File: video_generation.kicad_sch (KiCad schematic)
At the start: 34 parts, among them J12 28L22, J15 74LS161, K15 74LS04

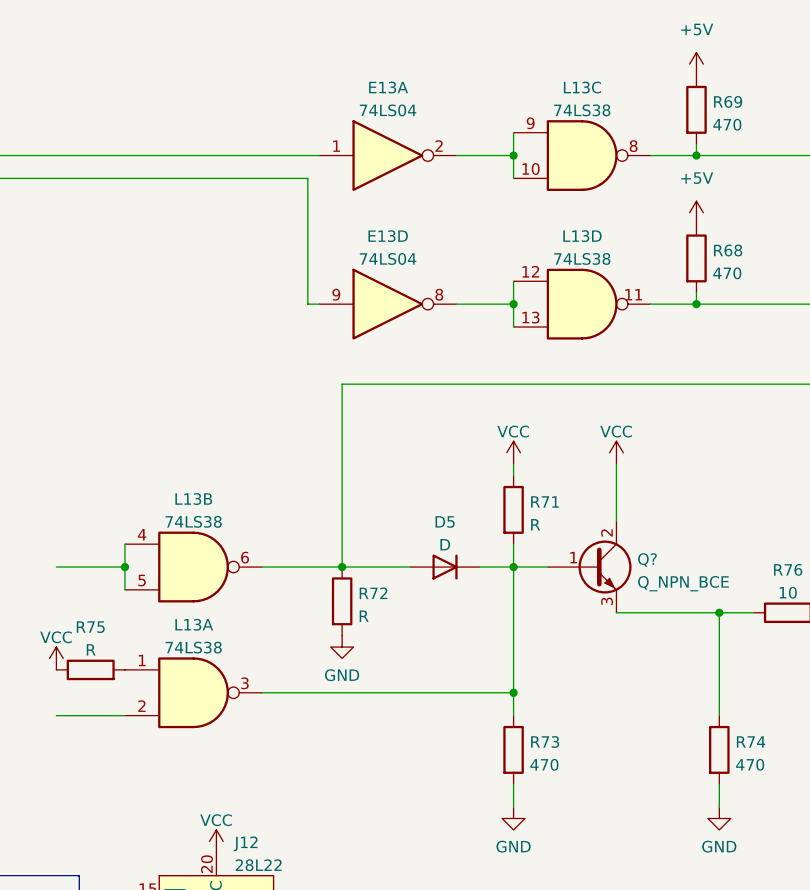
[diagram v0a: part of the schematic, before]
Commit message: Upgraded to kicad 7
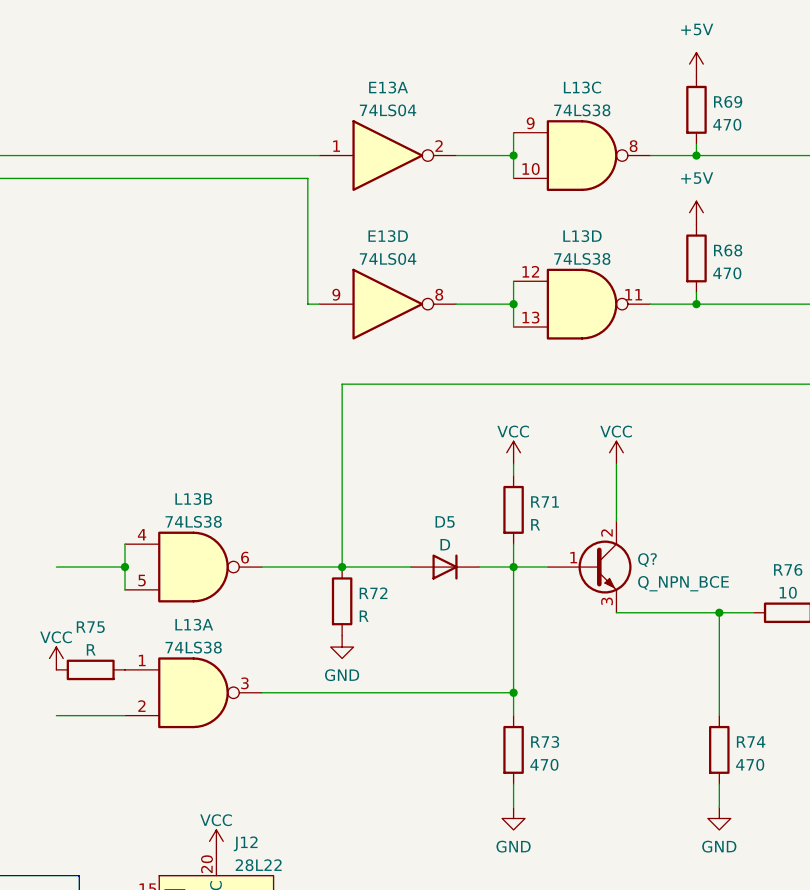
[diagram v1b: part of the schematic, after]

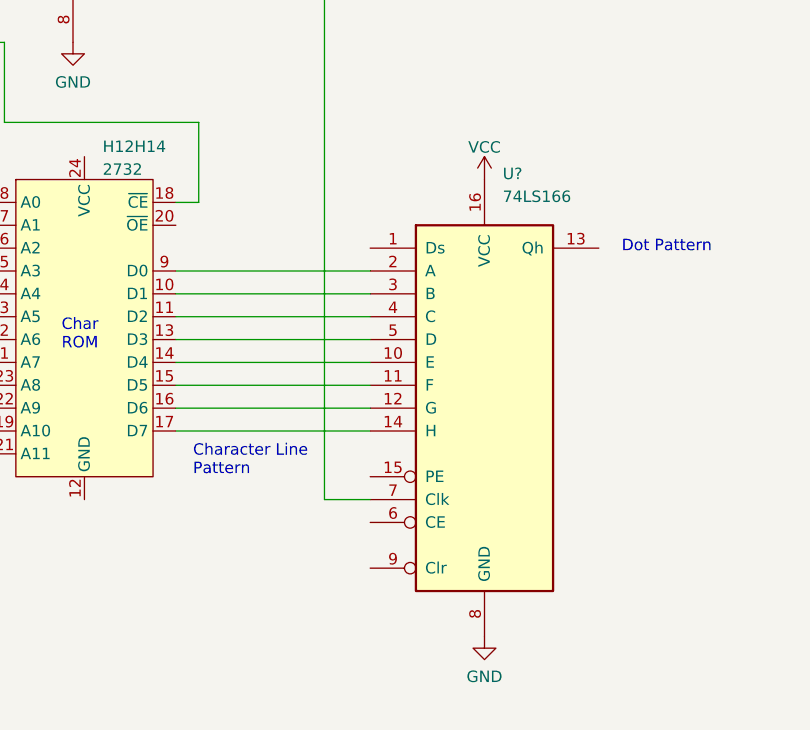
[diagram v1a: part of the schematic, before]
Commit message: Note in pixel shift register
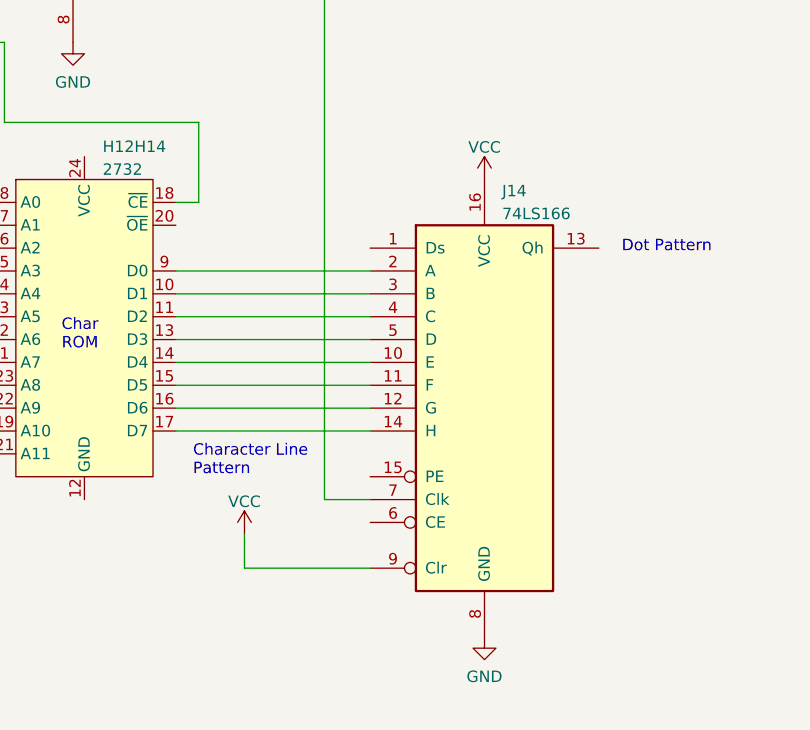
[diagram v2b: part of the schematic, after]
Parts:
- gave numbers to parts that had none: 1
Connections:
- net VCC: now also J14.9 (Clr)
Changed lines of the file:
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@@
+    (stroke (width 0) (type default))
+  )
+  (wire (pts (xy 252.73 198.12) (xy 238.76 198.12))
     (stroke (width 0) (type default))
   )
@@
   )
   (bus (pts (xy 25.4 238.76) (xy 25.4 246.38))
+    (stroke (width 0) (type default))
+  )
+  (wire (pts (xy 238.76 194.31) (xy 238.76 198.12))
     (stroke (width 0) (type default))
   )
@@
         (path "/12a6dbe3-008d-4c5b-88f6-9f1c816060be/ce60e45b-d802-4380-8f39-bef3de5fa20e"
           (reference "K15") (unit 4)
+        )
+      )
+    )
+  )
+  (symbol (lib_id "power:VCC") (at 238.76 194.31 0) (unit 1)
+    (in_bom yes) (on_board yes) (dnp no)
+    (property "Reference" "#PWR01" (at 238.76 198.12 0)
+      (effects (font (size 1.27 1.27)) hide)
+    )
+    (property "Value" "VCC" (at 238.76 190.7342 0)
+      (effects (font (size 1.27 1.27)))
+    )
+    (property "Footprint" "" (at 238.76 194.31 0)
+      (effects (font (size 1.27 1.27)) hide)
+    )
+    (property "Datasheet" "" (at 238.76 194.31 0)
+      (effects (font (size 1.27 1.27)) hide)
+    )
+    (pin "1")
+    (instances
+      (project "ceda"
+        (path "/12a6dbe3-008d-4c5b-88f6-9f1c816060be/ce60e45b-d802-4380-8f39-bef3de5fa20e"
+          (reference "#PWR01") (unit 1)
         )
       )
@@
   (symbol (lib_id "74xx:74LS166") (at 265.43 180.34 0) (unit 1)
     (in_bom yes) (on_board yes) (dnp no) (fields_autoplaced)
-    (property "Reference" "U?" (at 267.4494 154.305 0)
-      (effects (font (size 1.27 1.27)) (justify left))
-    )
-    (property "Value" "74LS166" (at 267.4494 156.845 0)
+    (property "Reference" "J14" (at 267.3859 156.21 0)
+      (effects (font (size 1.27 1.27)) (justify left))
+    )
+    (property "Value" "74LS166" (at 267.3859 158.75 0)
       (effects (font (size 1.27 1.27)) (justify left))
     )
@@
       (project "ceda"
         (path "/12a6dbe3-008d-4c5b-88f6-9f1c816060be/ce60e45b-d802-4380-8f39-bef3de5fa20e"
-          (reference "U?") (unit 1)
-        )
-      )
+          (reference "J14") (unit 1)
+        )
+      )

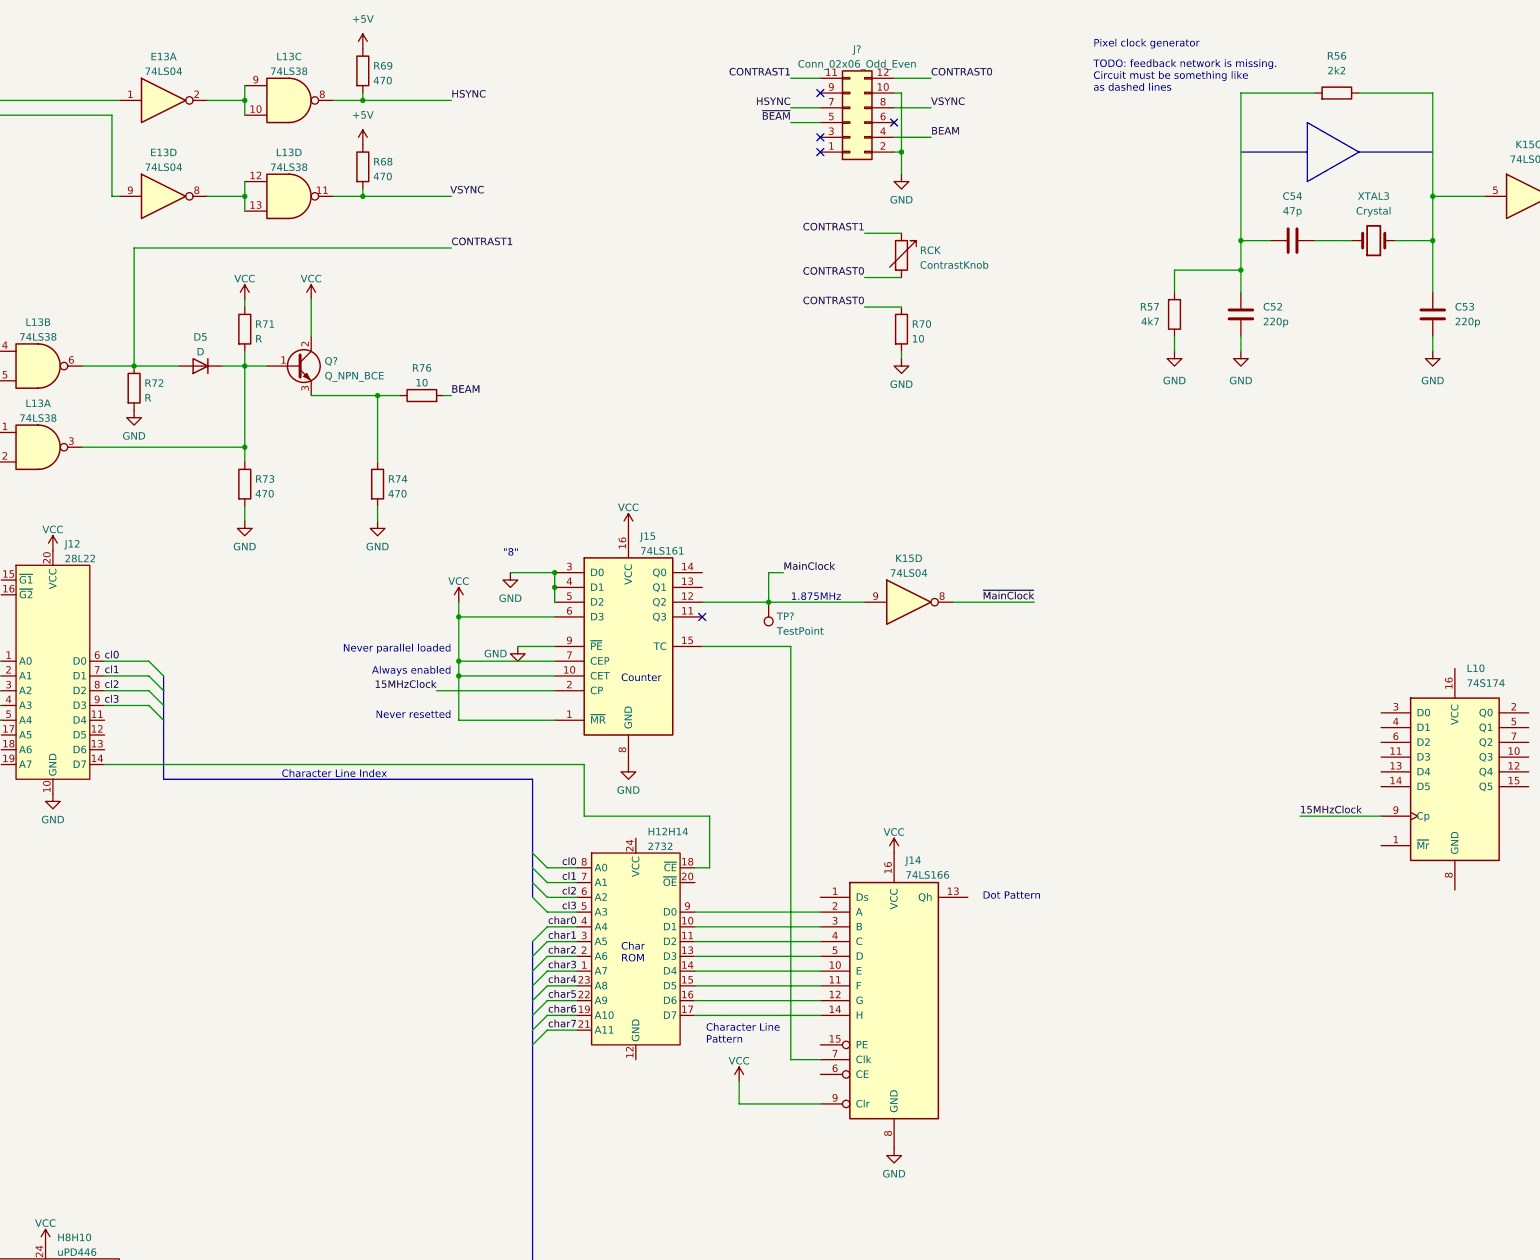
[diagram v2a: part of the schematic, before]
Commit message: Discovered bank 0 + fixed wrong signals in video gen
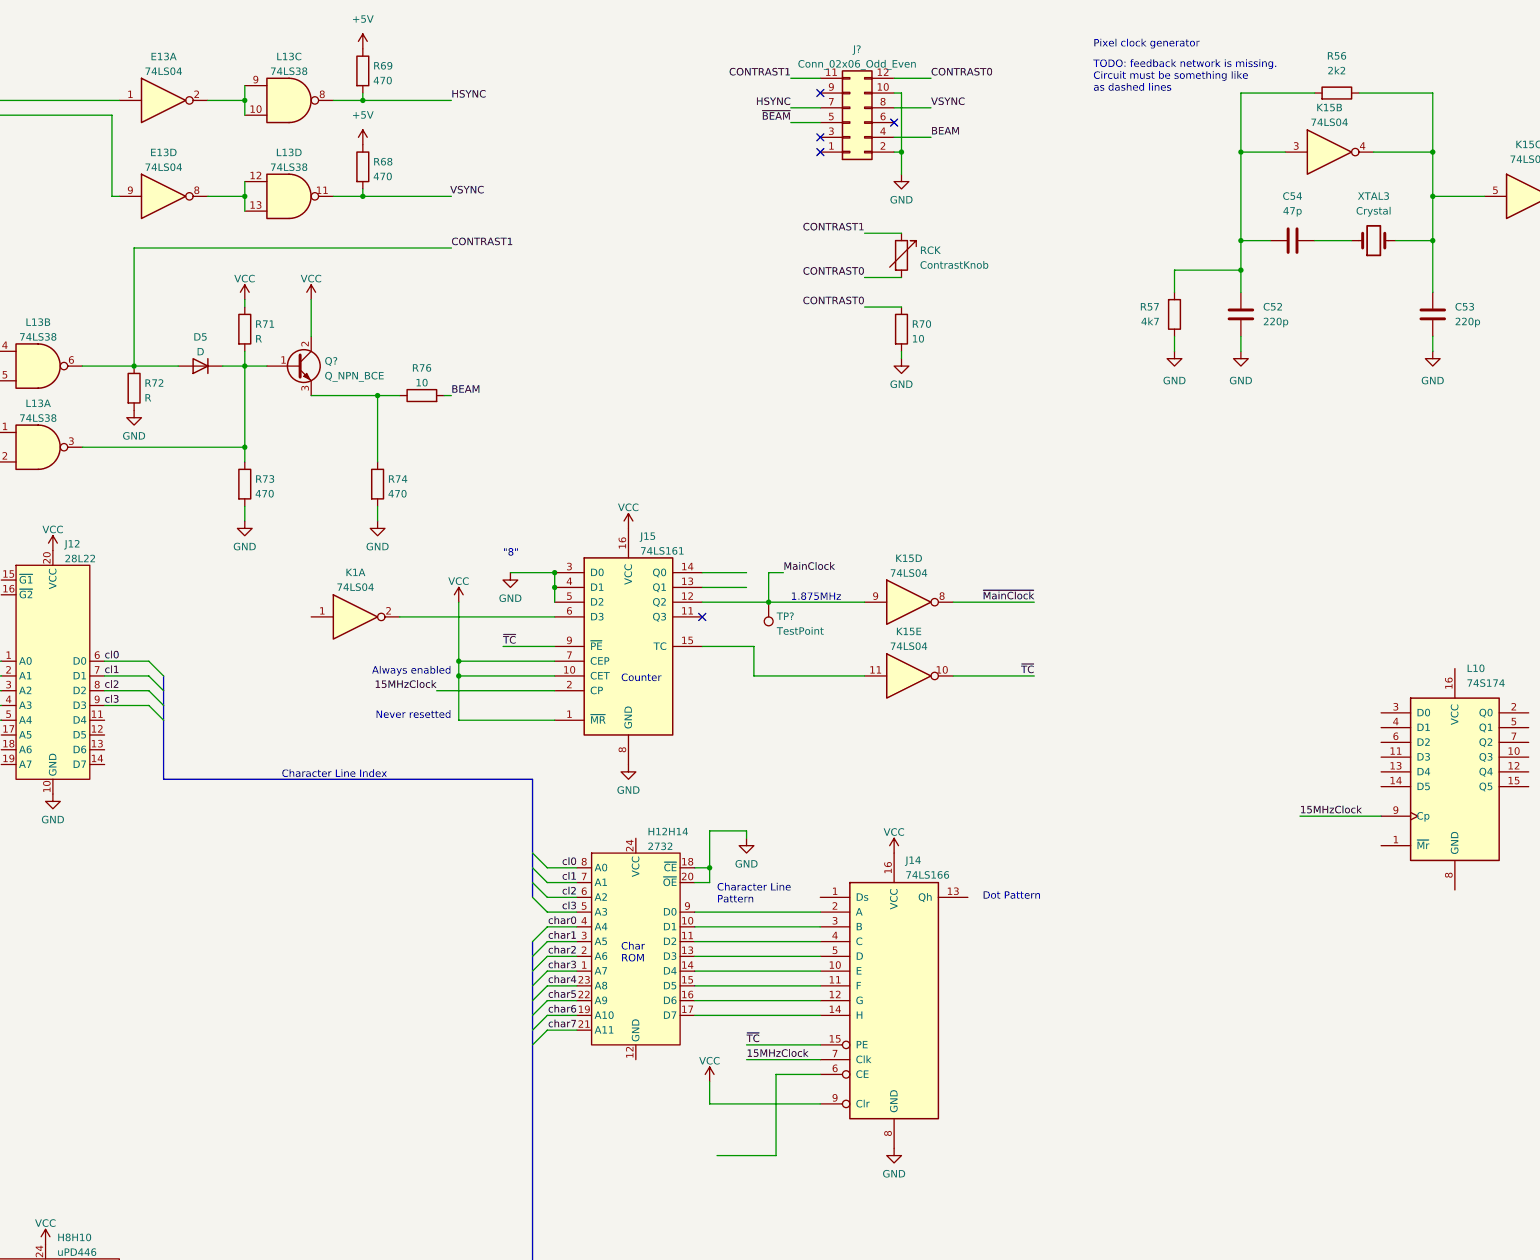
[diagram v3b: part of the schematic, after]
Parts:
- added K1: 74LS04, symbol 74xx:74LS04
- added unit 2 of K15
- added unit 5 of K15
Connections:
- net 15MHzClock: now also J14.7 (Clk)
- net GND: now also H12H14.18 (~{CE}), H12H14.20 (~{OE}); no longer J15.9 (~{PE})
- net VCC: no longer J15.6 (D3)
- net at J12.14 (D7): no longer H12H14.18 (~{CE})
- net at C53.1, K15.5, R56.1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: now also K15.4
- net at C52.1, C54.2, R56.2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: now also K15.3
- net at J15.15 (TC): now also K15.11; no longer J14.7 (Clk)
- net ~{TC}: now reaches J14.15 (PE)
- net ~{TC}: now also J15.9 (~{PE}), K15.10
- new net: J15.6 (D3), K1.2
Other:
- note removed: "Never parallel loaded"

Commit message: A long job in analog video output
! Read comments inside video_memory_management sheet for more
informations.

- Completed path between dot pattern output of character shift register
and beam output transistor.
- Found behavior of video attribute signals: blink, underline, stretch,
  hide.
- Completed wiring of 28L22 ROM, which is involved in video attributes.
- TODO: video_memory_management must be cleaned up, since schematics has grown
outside sheet.
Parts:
- added D2: D, symbol Device:D
- added E12: 74LS175, symbol 74xx:74LS175
- added J13: 74LS86, symbol 74xx:74LS86
- added K0000, L12, U14, U5: 74LS00, symbol 74xx:74LS00
- added K10, U3: 74LS08, symbol 74xx:74LS08
- added K11, K12: 74LS273, symbol 74xx:74LS273
- added K14, U2: 74LS10, symbol 74xx:74LS10
- added R67, R71: R, symbol Device:R
- added U1: 74LS393, symbol 74xx:74LS393
- added U4: 74LS04, symbol 74xx:74LS04
- gave numbers to parts that had none: 1
- renumbered K1 to K15
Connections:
- net GND: now also R71.2
- net MainClock: now also E12.9 (Cp), K11.11 (Cp)
- net ~{TC}: now also K12.11 (Cp)
- net at D5.1 (K), R71.2, R73.1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: now also D2.1 (K); no longer L13.3
- net disptmg: now reaches E7E11.18 (DISPTMG)
- net disptmg: now also E12.4 (D0)
- net cudisp: now reaches E7E11.19 (CUDISP)
- net cudisp: now also E12.12 (D2)
- net half_pxclk: now reaches J15.14 (Q0)
- net half_pxclk: now also U4.1
- net at L10.1 (~{Mr}): now also R67.2
- net pixel_reg: now reaches L10.2 (Q0)
- net pixel_reg: now also K10.2
- net pixel: now reaches L10.3 (D0)
- net pixel: now also J13.3
- net disptmg_reg: now reaches L10.4 (D1)
- net disptmg_reg: now also E12.7 (Q1)
- net disptmg_ancorpiureg: now reaches L10.5 (Q1)
- net disptmg_ancorpiureg: now also K10.1
- net attr_cursor: now reaches L10.6 (D2)
- net attr_cursor: now also K12.6 (Q2)
- net attr_cursor_reg: now reaches L10.7 (Q2)
- net attr_cursor_reg: now also L12.12, L12.4
- net at J14.6 (CE): now also U3.3
- net at L13.2: now also L12.3
- net at L13.4, L13.5: now also L12.11
- new net: J13.1, J13.6
- new net: K0000.6, K14.9
- new net: K11.12 (Q4), K12.13 (D4)
- new net: K11.5 (Q1), K12.4 (D1)
- new net: K11.6 (Q2), K12.7 (D2)
- new net: K11.9 (Q3), K12.8 (D3)
- new net: U1.13 (CP), U1.3 (Q0)
- new net: U3.1, U4.2
- new net: K14.4, U5.11
- new net: U14.8, U5.13
- new net: K10.3, L12.13, L12.2
- new net: L12.1, L12.6
- new net: D2.2 (A), L13.3, R71.1
- new net: K10.6, K11.13 (D4)
- new net: K14.3, K14.5, K14.8
- new net: J13.5, K14.6
- new net attr_blink: K0000.5, K12.5 (Q1)
- new net attr_blink_underline: K12.15 (Q5), U14.9
- new net attr_data0: K11.8 (D3)
- new net attr_data1: K11.4 (D1)
- new net attr_data2: K11.7 (D2)
- new net attr_data3: K10.5
- new net attr_data4: K11.17 (D6)
- new net attr_data5: K11.18 (D7)
- new net attr_data6: K11.14 (D5)
- new net attr_data7: K11.3 (D0)
- new net attr_hide: K12.19 (Q7), K14.11
- new net attr_invert: J13.4, K12.9 (Q3)
- new net attr_stretch: K12.12 (Q4), U3.2
- new net attr_underline: K12.16 (Q6), U5.12
- new net blink timer: K0000.4, U1.8 (Q3), U14.10
- new net cudisp_int: E12.10 (Q2), E12.13 (D3)
- new net cudisp_reg: E12.15 (Q3), J13.2
- new net disptmg_int: E12.2 (Q0), E12.5 (D1)
- new net dot pattern: K14.10
- new net ~{VSYNC_CRTC}: U1.1 (CP)
- new net ~{cudisp_reg}: E12.14 (~{Q3}), L12.5
- no-connect marks 10 -> 28
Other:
- note added: "1/32 VSYNC ~ 1.28s"
- note added: "174"
- note added: "All video data occurring during blanking time must be ignored. DISPTMG is 0 during blanking time."
- note added: "Blink generator"
- note added: "D0 from attribute RAM is "invert": when 1, frame is displayed in inverted colors."
- note added: "D2 from attribute RAM is "cursor enable": - If D2 is 0, CUDISP is gated by L12B. Character video can reach BEAM through L12A -> L13A. - If D2 is 1, CUDISP is no more gated and can be mixed with character video in L12A. The purpose of L12D -> L13B is unclear, since character video can already reach BEAM through the other path."
- note added: "D5 from ROM is "show": when 0, it gates dot_pattern video signal from the shift register. D1 from ROM is "blink": - when 0, it gates blink_timer and dot_pattern is not affected. - when 1, blink_timer can gate dot_pattern, making the character appear and disappear. blink_timer is a square wave obtained from VSYNC / 32 ~ 1.28s"
- note added: "D6 from ROM is "underline" ROM is both addressed with raster address wires (RA) and some attribute RAM outputs. When attribute RAM D4 = 1 we have this D6 from ROM = 1 on RA=13, else 0, resulting in an undeline effect. Note that "underline" is not affected by "blink" nor "show". D7 from ROM must be set to make the cursor blink too."
- note added: "EXT pad"
- note added: "Handling "stretch attribute": - When stretch attribute is 0, the shift register is always enabled; - When stretch attribute is 1, the shift register is enabled one clock in two."
- note added: "ROM_A5"
- note added: "ROM_A6"
- note added: "ROM_A7"
- note added: "ROM_D5"
- note added: "ROM_D6"
- note added: "ROM_D7"
- note added: "Toggle pixels when cursor has to be shown."
- note added: "VERIFY"
- note added: "Wired OR"
- note added: "With high probability this is strech at first register barrier (K12 pin 13)"
- note added: "registered ATTR RAM D0"
- note added: "registered ATTR RAM D1"
- note added: "registered D2 attr ram"
- note added: "registered D5 ROM"
- note added: "registered D6 ROM"
- note added: "registered D7 ROM"
- moved on the sheet: D5, L13A, L13B, R71, R72, R73, R74, R75, R76, TR4

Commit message: Other steps in video generation
- Some notes regarding video attributes.
- Found some stuck-at inputs.
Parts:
- renumbered U1 to L11
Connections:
- net GND: now also F10.15 (E), F8.15 (E), F9.15 (E), J12.15 (~{G1}), J12.16 (~{G2}), J14.1 (Ds), L11.12 (MR), L11.2 (MR)
- net VCC: now also K11.1 (~{Mr}), K12.1 (~{Mr})
- net ~{RESET}: now reaches E7E11.2 (~{RES})
- no-connect marks 28 -> 29
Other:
- note added: "(pixel_reg and disptmg) and attr_cursor or (pixel_reg and disptmg) and (~attr_cursor or cudisp)"
- note added: "D2 from attribute RAM is something related to cursor"
- note added: "Toggle pixels when cursor has to be shown. If characher is inverted, cursor is inverted too."
- note added: "Wired OR. Transistor base is pulled up (i.e. BEAM is pulled up) if L13B is HIGH or L13A is HIGH."
- note removed: "D2 from attribute RAM is "cursor enable": - If D2 is 0, CUDISP is gated by L12B. Character video can reach BEAM through L12A -> L13A. - If D2 is 1, CUDISP is no more gated and can be mixed with character video in L12A. The purpose of L12D -> L13B is unclear, since character video can already reach BEAM through the other path."
- note removed: "Toggle pixels when cursor has to be shown."
- note removed: "Wired OR"
- moved on the sheet: L11B
